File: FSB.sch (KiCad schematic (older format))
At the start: 11 parts

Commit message: added esp, usb/uart ic, program circuit
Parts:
- added C? (x3): C_Small, symbol Device:C_Small
- added Q? (x2): MMBT3904, Package_TO_SOT_SMD:SOT-23, symbol Transistor_BJT:MMBT3904
- added R? (x2): 10k, symbol Device:R_Small
- added R? (x2): 10K, symbol Device:R_Small
- added SW?: SW_Push, symbol Switch:SW_Push
- added U?: ESP-12F, RF_Module:ESP-12E, symbol RF_Module:ESP-12F
- added U?: CY7C65213-32LTXI, Package_DFN_QFN:QFN-32-1EP_5x5mm_P0.5mm_EP3.45x3.45mm, symbol Interface_USB:CY7C65213-32LTXI
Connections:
- net labels added: +3.3V, DTR, EN, GPIO0, RST, RTS, VBUS, ~RST~
- wire segments 36 -> 92

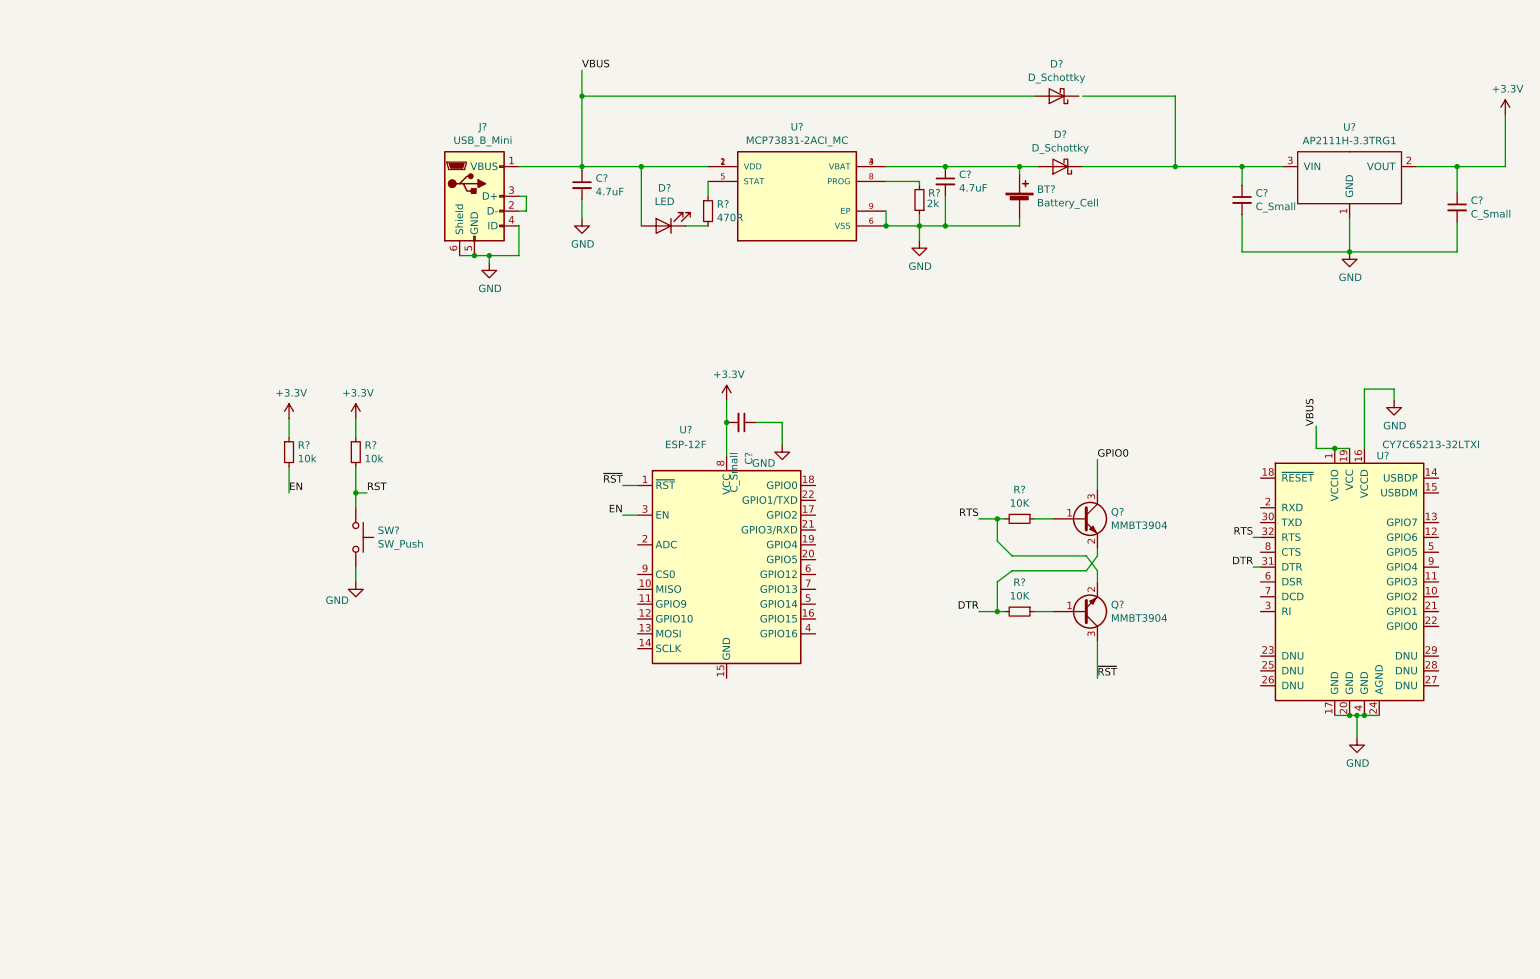
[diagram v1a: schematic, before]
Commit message: ADDED H BRIDGE ID AND FTDI HEADER
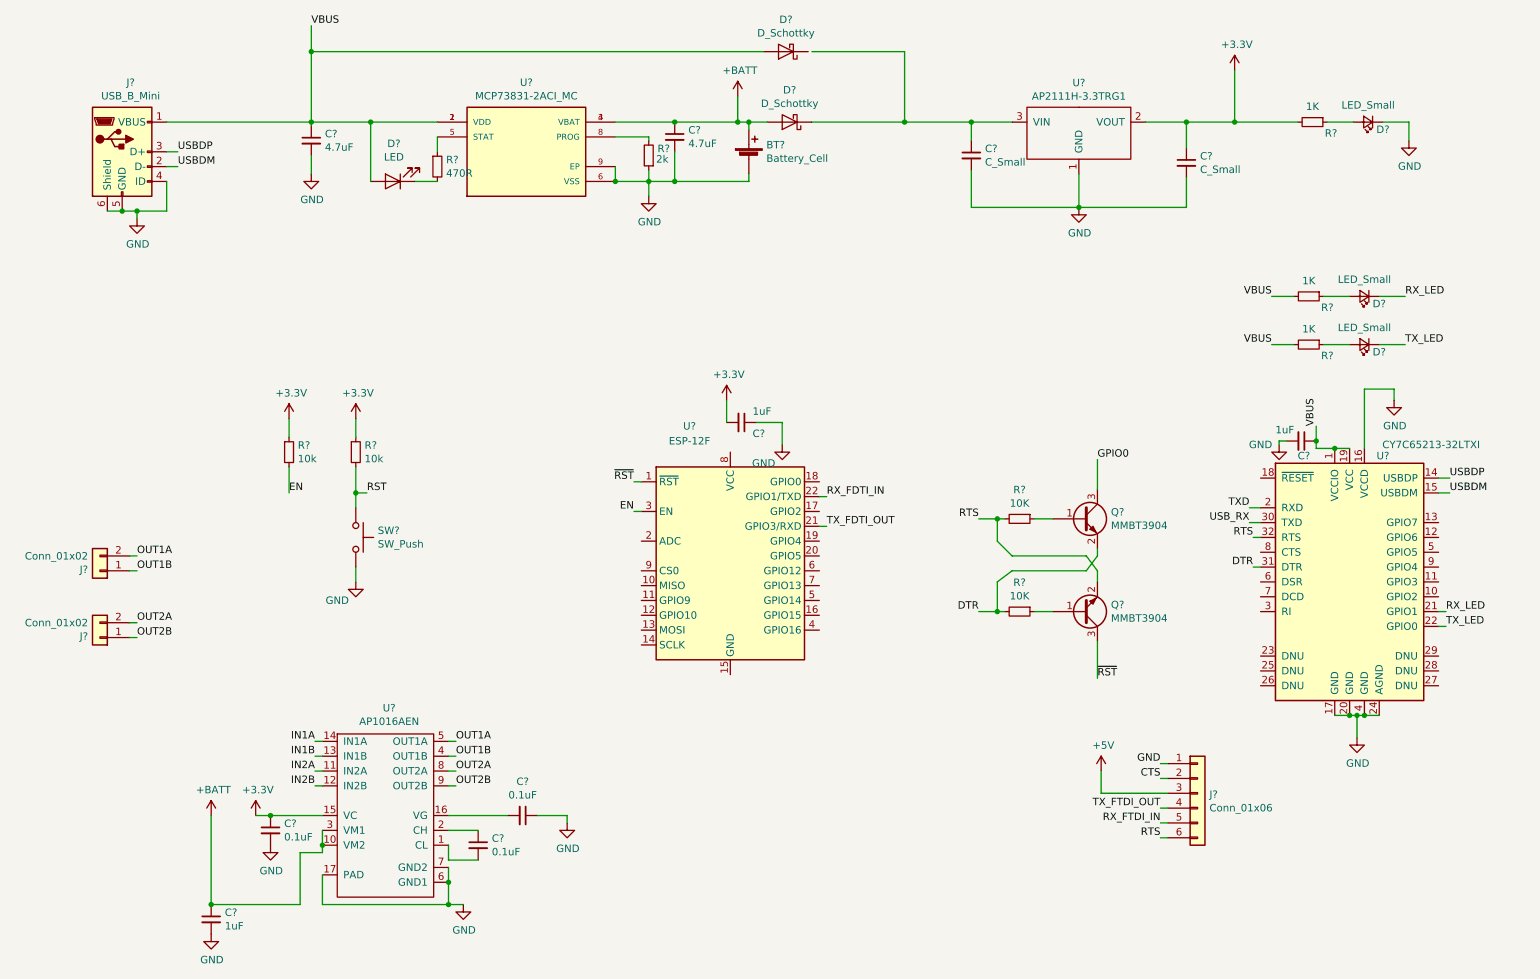
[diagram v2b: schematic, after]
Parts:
- added C? (x2): 1uF, symbol Device:C_Small
- added C? (x3): 0.1uF, symbol Device:C_Small
- added D? (x3): LED_Small, symbol Device:LED_Small
- added J? (x2): Conn_01x02, symbol Connector_Generic:Conn_01x02
- added J?: Conn_01x06, symbol Connector_Generic:Conn_01x06
- added R? (x3): 1K, symbol Device:R_Small
- added U?: AP1016AEN, symbol Kicad_symbols:AP1016AEN
- C?: value C_Small -> 1uF
- J?: footprint (none) -> Connector_USB:USB_Mini-B_Wuerth_65100516121_Horizontal
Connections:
- net +3V3: now also C?.1, R?.2, U?.15 (VC); no longer U?.8 (VCC)
- net GND: now also C?.1, C?.2, C?.2, C?.2, D?.1 (K), J?.1 (Pin_1), U?.17 (PAD), U?.6 (GND1), U?.7 (GND2)
- net RTS: now also J?.6 (Pin_6)
- net VBUS: now also C?.1, R?.2, R?.2
- net +BATT: now reaches BT?.1 (+), C?.1, D?.2 (A), U?.3 (VBAT), U?.4 (VBAT)
- net +BATT: now also C?.1, U?.10 (VM2), U?.3 (VM1)
- net USBDM: now reaches J?.2 (D-)
- net USBDM: now also U?.15 (USBDM); no longer J?.3 (D+)
- net TX_FDTI_OUT: now reaches U?.21 (GPIO3/RXD)
- net RX_FDTI_IN: now reaches U?.22 (GPIO1/TXD)
- net USBDP: now reaches U?.14 (USBDP)
- net USBDP: now also J?.3 (D+)
- net TXD: now reaches U?.2 (RXD)
- net RX_LED: now reaches U?.21 (GPIO1)
- net RX_LED: now also D?.1 (K)
- net TX_LED: now reaches U?.22 (GPIO0)
- net TX_LED: now also D?.1 (K)
- net USB_RX: now reaches U?.30 (TXD)
- new net: D?.2 (A), R?.1 (x3)
- new net: C?.2, U?.1 (CL)
- new net: C?.2, U?.16 (VG)
- new net: C?.1, U?.2 (CH)
- new net +5V: J?.3 (Pin_3)
- new net CTS: J?.2 (Pin_2)
- new net IN1A: U?.14 (IN1A)
- new net IN1B: U?.13 (IN1B)
- new net IN2A: U?.11 (IN2A)
- new net IN2B: U?.12 (IN2B)
- new net OUT1A: J?.2 (Pin_2), U?.5 (OUT1A)
- new net OUT1B: J?.1 (Pin_1), U?.4 (OUT1B)
- new net OUT2A: J?.2 (Pin_2), U?.8 (OUT2A)
- new net OUT2B: J?.1 (Pin_1), U?.9 (OUT2B)
- new net RX_FTDI_IN: J?.5 (Pin_5)
- new net TX_FTDI_OUT: J?.4 (Pin_4)
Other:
- moved on the sheet: BT?, C?, D?, J?, R?, U?
